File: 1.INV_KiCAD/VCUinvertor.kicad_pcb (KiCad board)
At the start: 2 copper layers, 100.7 x 138.5 mm, 160 parts, among them J10 FAN2, J11 PUMP1, J12 PUMP2, J7 PowerSupply, J8 FAN1, J9 BRAKE LIGHT, K1 IM06DGR, Q1 2N7002, Q10 2N7002, Q11 2N7002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

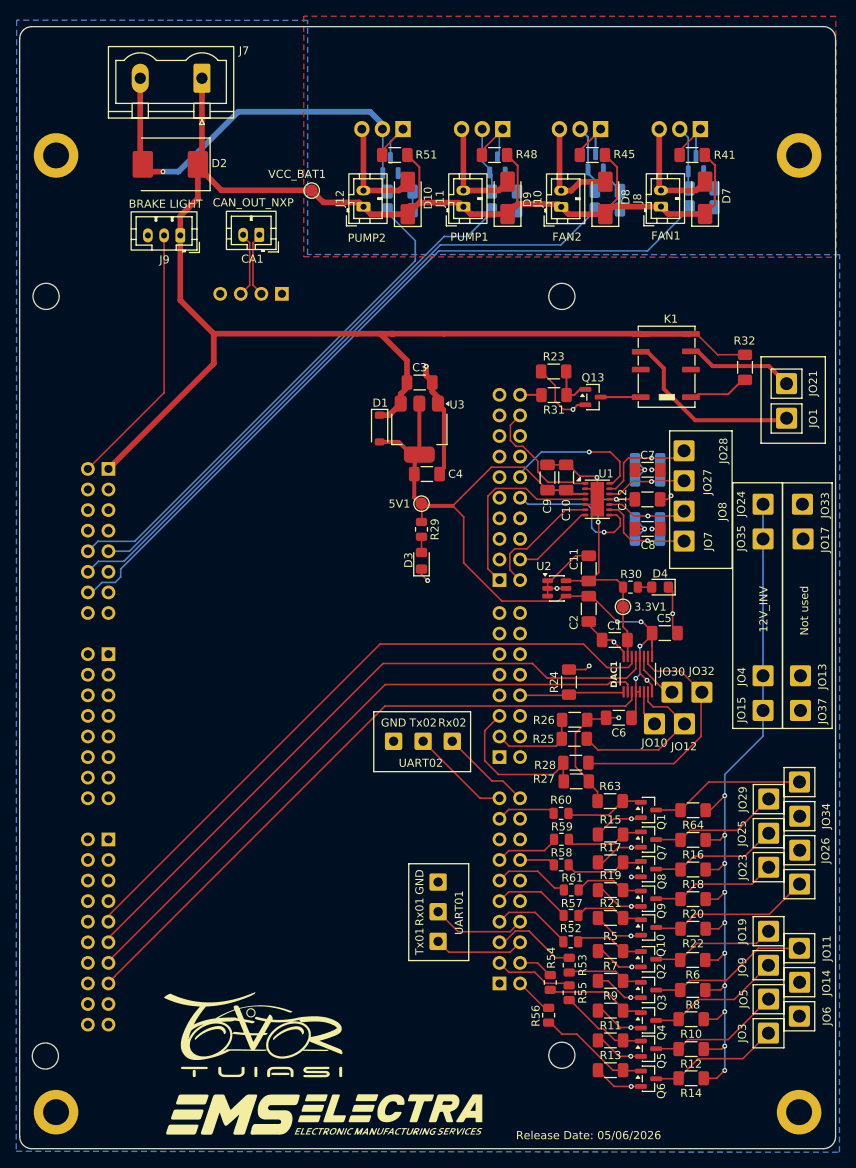
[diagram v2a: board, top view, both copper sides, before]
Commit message: Mounting Holes + Relay Flyback added
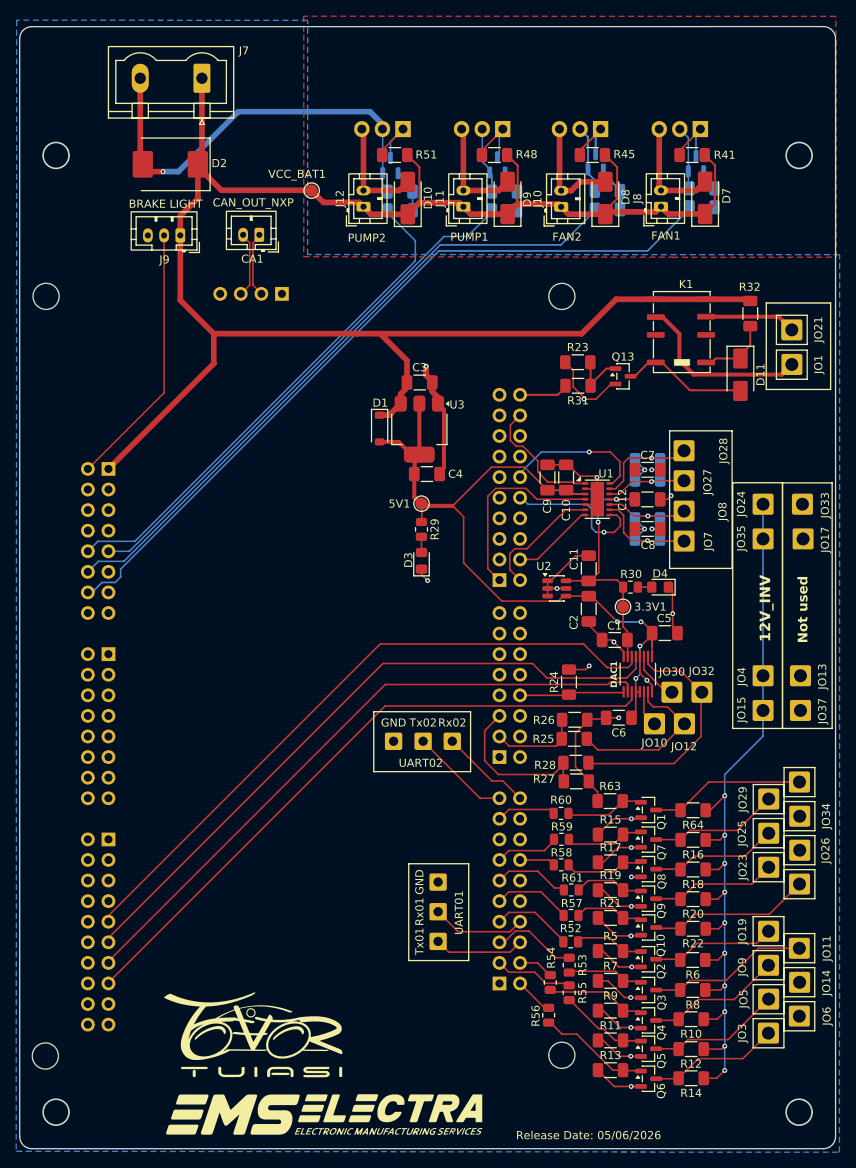
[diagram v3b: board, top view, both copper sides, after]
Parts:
- removed H1, H2, H3, H4: MountingHole_Pad, MountingHole:MountingHole_3.2mm_M3_ISO14580_Pad
- added D11: SS34, Diode_SMD:D_SMA, F.Cu at (141.0, 71.4)
- R23: value 10k -> 47k
- moved JO1 6.67 mm to (147.4, 70.1)
- moved JO21 6.67 mm to (147.4, 65.9)
- moved R32 6.67 mm to (142.2, 63.9)
- moved K1 4.67 mm to (131.6, 65.7)
- moved Q13 4.51 mm to (126.5, 71.6)
- moved R23 3.18 mm to (120.9, 69.9)
- moved R31 3.18 mm to (121.0, 72.8)
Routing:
- net Net-(D11-A): track 4.95 -> 15.7 mm
- net INV_OFF: track 2.65 -> 6.17 mm
- net /INV2_Vcc: track 13.5 -> 11.3 mm
- net Net-(D11-K): track 7.56 -> 9.17 mm
- net Net-(Q13-B): track 5.54 -> 6.96 mm
- net GND: track 227.2 -> 228.7 mm
- net BAT+: track 235.8 -> 236.8 mm
- net /INV1_Vcc: track 23.1 -> 22.2 mm
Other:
- outline, holes or cut-outs redrawn

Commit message: Connectors 2.0mm -> 2.5mm correction
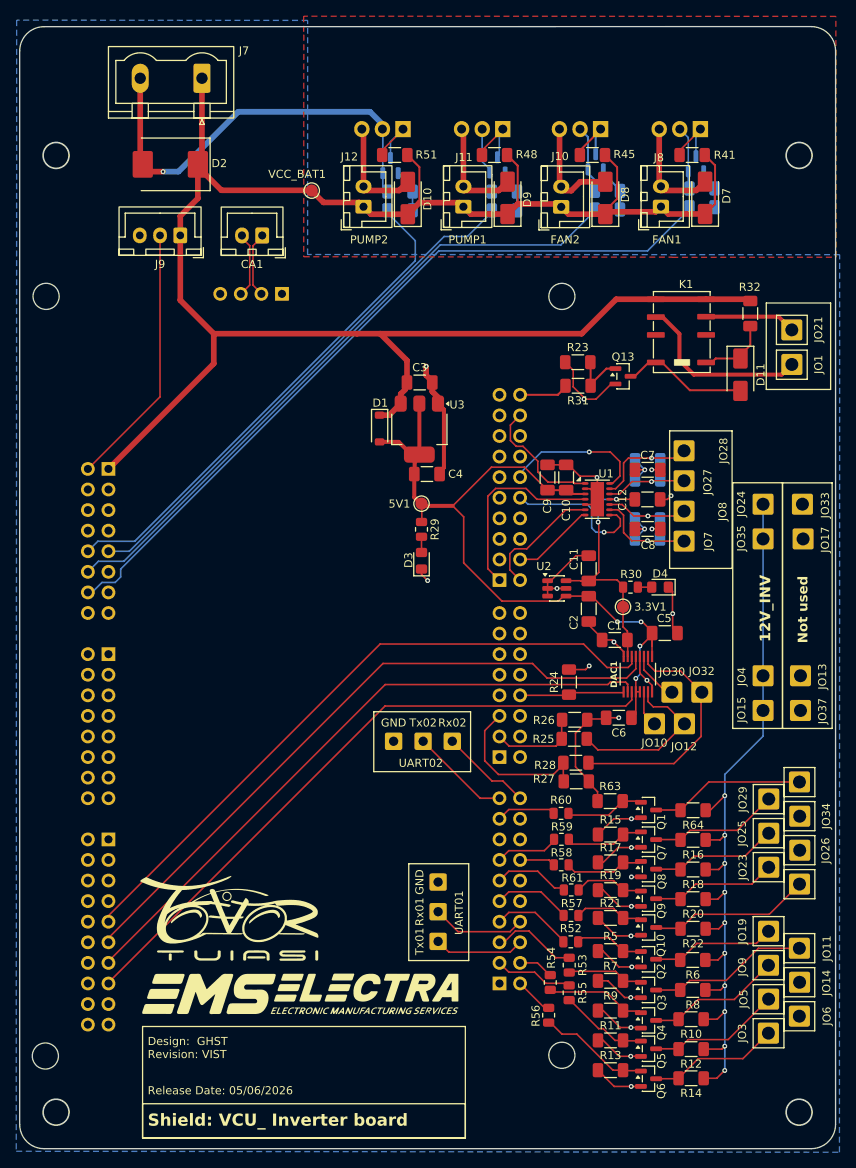
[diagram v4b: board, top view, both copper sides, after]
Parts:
- CA1, J10, J11, J12, J8: footprint Connector_JST:JST_PH_B2B-PH-K_1x02_P2.00mm_Vertical -> Connector_JST:JST_XH_B2B-XH-A_1x02_P2.50mm_Vertical
- J9: footprint Connector_JST:JST_PH_B3B-PH-K_1x03_P2.00mm_Vertical -> Connector_JST:JST_XH_B3B-XH-A_1x03_P2.50mm_Vertical
- moved G*** 14.7 mm to (77.9, 138.5)
- moved CA1 0.36 mm to (82.0, 54.2)
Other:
- outline, holes or cut-outs redrawn
- board text added: "Design: GHST Revision: VIST"
- board text added: "Shield: VCU_ Inverter board"

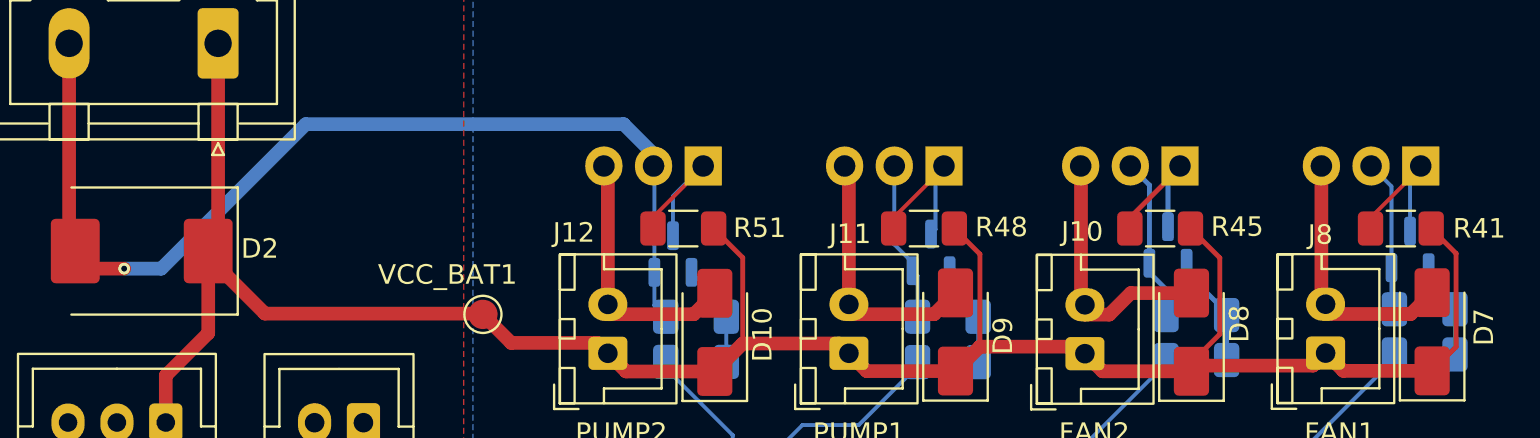
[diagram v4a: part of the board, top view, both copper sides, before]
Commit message: FAN MOS correction D->S
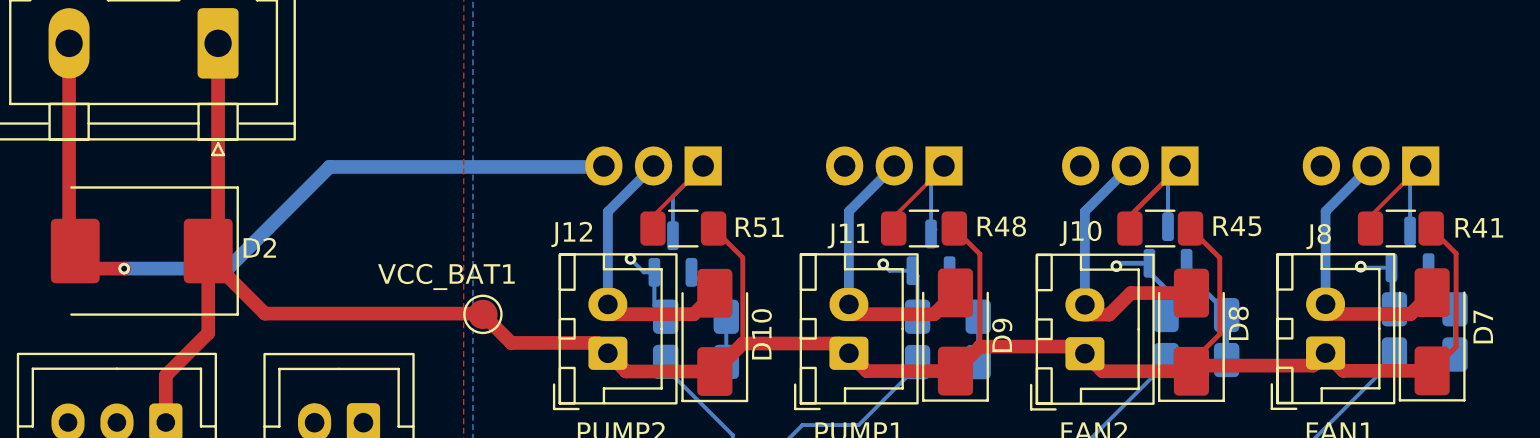
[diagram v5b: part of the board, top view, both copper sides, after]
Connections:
- Q15 pad 2: GND -> Net-(D7-A)
- Q15 pad 3: Net-(D7-A) -> GND
- Q16 pad 2: GND -> Net-(D8-A)
- Q16 pad 3: Net-(D8-A) -> GND
- Q17 pad 2: GND -> Net-(D9-A)
- Q17 pad 3: Net-(D9-A) -> GND
- Q19 pad 2: GND -> Net-(D10-A)
- Q19 pad 3: Net-(D10-A) -> GND
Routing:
- net GND: track 228.7 -> 209.3 mm, vias 24 -> 28
- net Net-(D7-A): track 13.6 -> 14.6 mm
- net Net-(Q14-D): track 8.02 -> 8.90 mm
- net Net-(Q12-D): track 7.96 -> 8.67 mm
- net Net-(D8-A): track 13.6 -> 14.3 mm

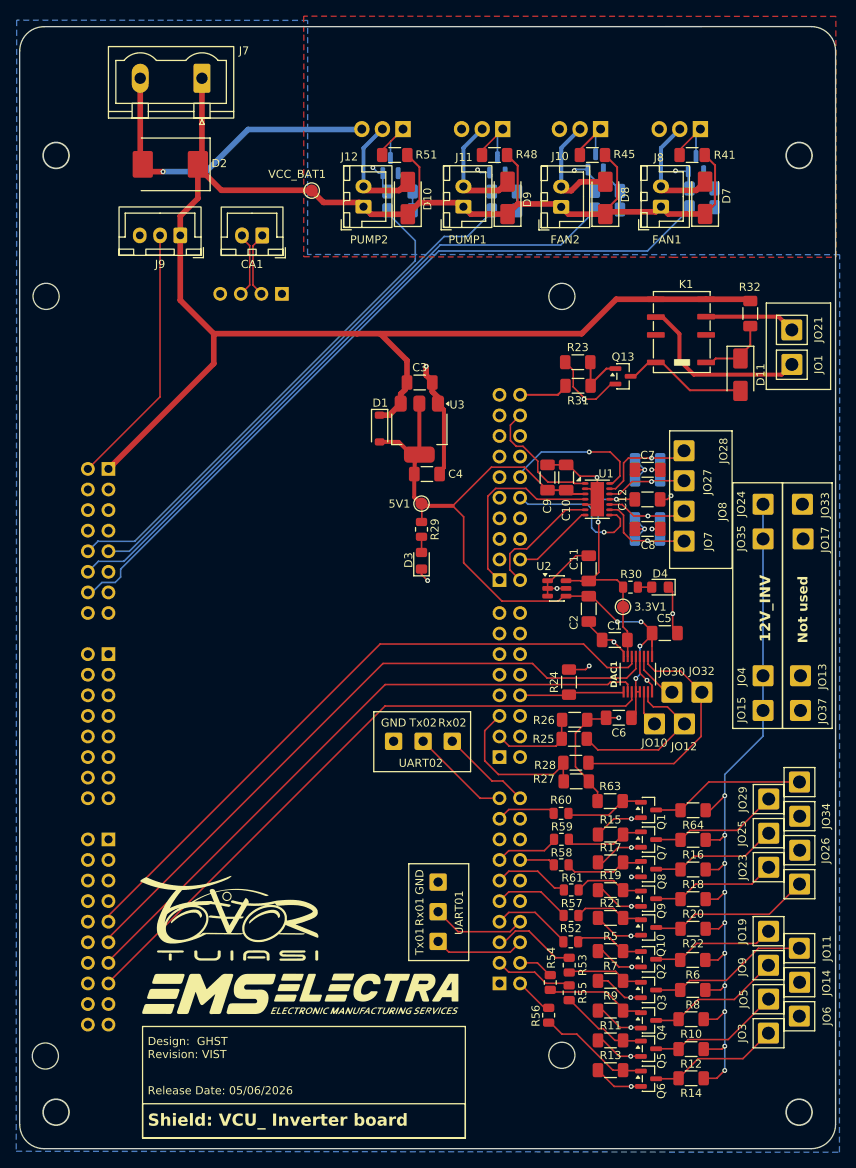
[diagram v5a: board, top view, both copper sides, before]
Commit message: Gate Driver MOS added + layout done
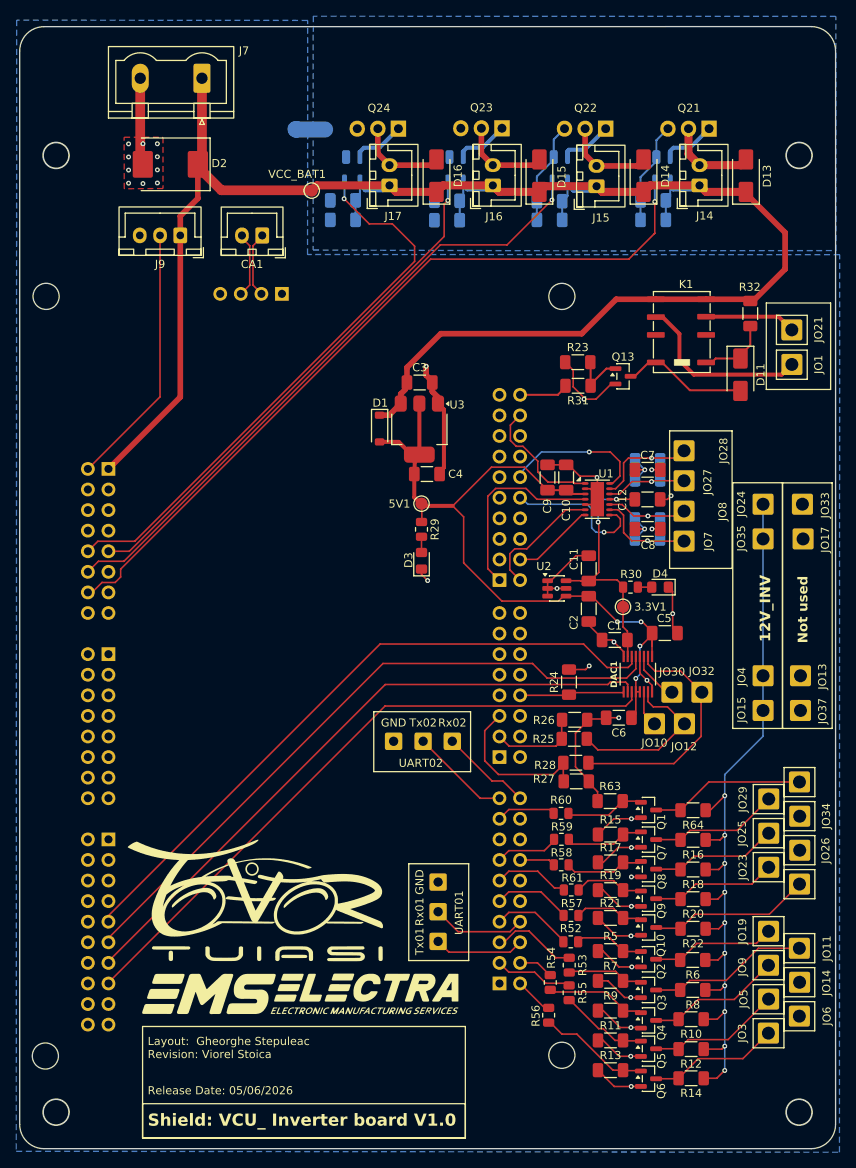
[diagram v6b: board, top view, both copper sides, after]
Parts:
- removed D10, D7, D8, D9: SS34, Diode_SMD:D_SMA
- removed J10: FAN2, Connector_JST:JST_XH_B2B-XH-A_1x02_P2.50mm_Vertical
- removed J11: PUMP1, Connector_JST:JST_XH_B2B-XH-A_1x02_P2.50mm_Vertical
- removed J12: PUMP2, Connector_JST:JST_XH_B2B-XH-A_1x02_P2.50mm_Vertical
- removed J8: FAN1, Connector_JST:JST_XH_B2B-XH-A_1x02_P2.50mm_Vertical
- removed Q11, Q12, Q14, Q18: 2N7002, Package_TO_SOT_SMD:SOT-23
- removed Q15, Q16, Q17, Q19: IRLZ44N, Package_TO_SOT_THT:TO-220-3_Vertical
- removed R40, R47, R50: 100k, Resistor_SMD:R_1206_3216Metric_Pad1.30x1.75mm_HandSolder
- removed R41, R45, R48, R51: 47k, Resistor_SMD:R_1206_3216Metric_Pad1.30x1.75mm_HandSolder
- removed R42, R43, R46, R49: 100R, Resistor_SMD:R_1206_3216Metric_Pad1.30x1.75mm_HandSolder
- removed R44: 10k, Resistor_SMD:R_1206_3216Metric_Pad1.30x1.75mm_HandSolder
- added C15: 4.7uF, Capacitor_SMD:C_1206_3216Metric_Pad1.33x1.80mm_HandSolder, B.Cu at (130.2, 52.3)
- added C16: 0.1uF, Capacitor_SMD:C_1206_3216Metric_Pad1.33x1.80mm_HandSolder, B.Cu at (130.2, 49.9)
- added C17: 4.7uF, Capacitor_SMD:C_1206_3216Metric_Pad1.33x1.80mm_HandSolder, B.Cu at (117.5, 50.0)
- added C18: 0.1uF, Capacitor_SMD:C_1206_3216Metric_Pad1.33x1.80mm_HandSolder, B.Cu at (117.5, 52.3)
- added C19: 4.7uF, Capacitor_SMD:C_1206_3216Metric_Pad1.33x1.80mm_HandSolder, B.Cu at (104.8, 52.3)
- added C20: 0.1uF, Capacitor_SMD:C_1206_3216Metric_Pad1.33x1.80mm_HandSolder, B.Cu at (104.8, 49.9)
- added C21: 4.7uF, Capacitor_SMD:C_1206_3216Metric_Pad1.33x1.80mm_HandSolder, B.Cu at (92.0, 52.3)
- added C22: 0.1uF, Capacitor_SMD:C_1206_3216Metric_Pad1.33x1.80mm_HandSolder, B.Cu at (92.0, 49.9)
- added D13: SS34, Diode_SMD:D_SMA, F.Cu at (141.7, 46.8)
- added D14: SS34, Diode_SMD:D_SMA, F.Cu at (129.1, 46.8)
- added D15: SS34, Diode_SMD:D_SMA, F.Cu at (116.2, 46.8)
- added D16: SS34, Diode_SMD:D_SMA, F.Cu at (103.5, 46.8)
- added J14: FAN1, Connector_JST:JST_XH_B2B-XH-A_1x02_P2.50mm_Vertical, F.Cu at (136.0, 48.0)
- added J15: FAN2, Connector_JST:JST_XH_B2B-XH-A_1x02_P2.50mm_Vertical, F.Cu at (123.3, 48.1)
- added J16: PUMP1, Connector_JST:JST_XH_B2B-XH-A_1x02_P2.50mm_Vertical, F.Cu at (110.5, 48.0)
- added J17: PUMP2, Connector_JST:JST_XH_B2B-XH-A_1x02_P2.50mm_Vertical, F.Cu at (97.7, 48.0)
- added Q21: IRLZ44N, Package_TO_SOT_THT:TO-220-3_Vertical, B.Cu at (137.1, 41.0)
- added Q22: IRLZ44N, Package_TO_SOT_THT:TO-220-3_Vertical, B.Cu at (124.4, 41.0)
- added Q23: IRLZ44N, Package_TO_SOT_THT:TO-220-3_Vertical, B.Cu at (111.6, 41.0)
- added Q24: IRLZ44N, Package_TO_SOT_THT:TO-220-3_Vertical, B.Cu at (98.8, 41.0)
- added U5: MIC4416 BM4, Package_TO_SOT_SMD:SOT-143_Handsoldering, B.Cu at (131.4, 46.0)
- added U6: MIC4416 BM4, Package_TO_SOT_SMD:SOT-143_Handsoldering, B.Cu at (118.7, 46.0)
- added U7: MIC4416 BM4, Package_TO_SOT_SMD:SOT-143_Handsoldering, B.Cu at (105.9, 46.0)
- added U8: MIC4416 BM4, Package_TO_SOT_SMD:SOT-143_Handsoldering, B.Cu at (93.1, 46.0)
- moved G*** 3.90 mm to (81.2, 136.3)
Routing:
- net GND: track 209.3 -> 191.8 mm, vias 28 -> 33
- net Net-(D7-A): track 14.6 -> 0.00 mm
- net Net-(D8-A): track 14.3 -> 0.00 mm
- net Net-(D9-A): track 13.9 -> 0.00 mm
- net Net-(D10-A): track 13.8 -> 0.00 mm
- net Net-(D14-A): track 0.00 -> 11.3 mm
- net Net-(D16-A): track 0.00 -> 11.2 mm
- net Net-(D15-A): track 0.00 -> 11.2 mm
- net Net-(D13-A): track 0.00 -> 11.1 mm
- net Net-(Q14-D): track 8.90 -> 0.00 mm
- net Net-(Q12-D): track 8.67 -> 0.00 mm
- net Net-(Q18-D): track 8.52 -> 0.00 mm
- net Net-(Q11-D): track 7.90 -> 0.00 mm
- net /PUMP2: track 62.9 -> 70.3 mm, vias 0 -> 1
- net Net-(Q21-G): track 0.00 -> 6.69 mm
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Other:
- board text added: "Layout: Gheorghe Stepuleac Revision: Viorel Stoica"
- board text added: "Shield: VCU_ Inverter board V1.0"
- board text removed: "Design: GHST Revision: VIST"
- board text removed: "Shield: VCU_ Inverter board"
